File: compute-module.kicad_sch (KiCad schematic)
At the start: 16 parts, among them J7 DSI, SW1 SW_Push, SW2 SW_Push, U2 74154, U8 74LVC1G07SE-7

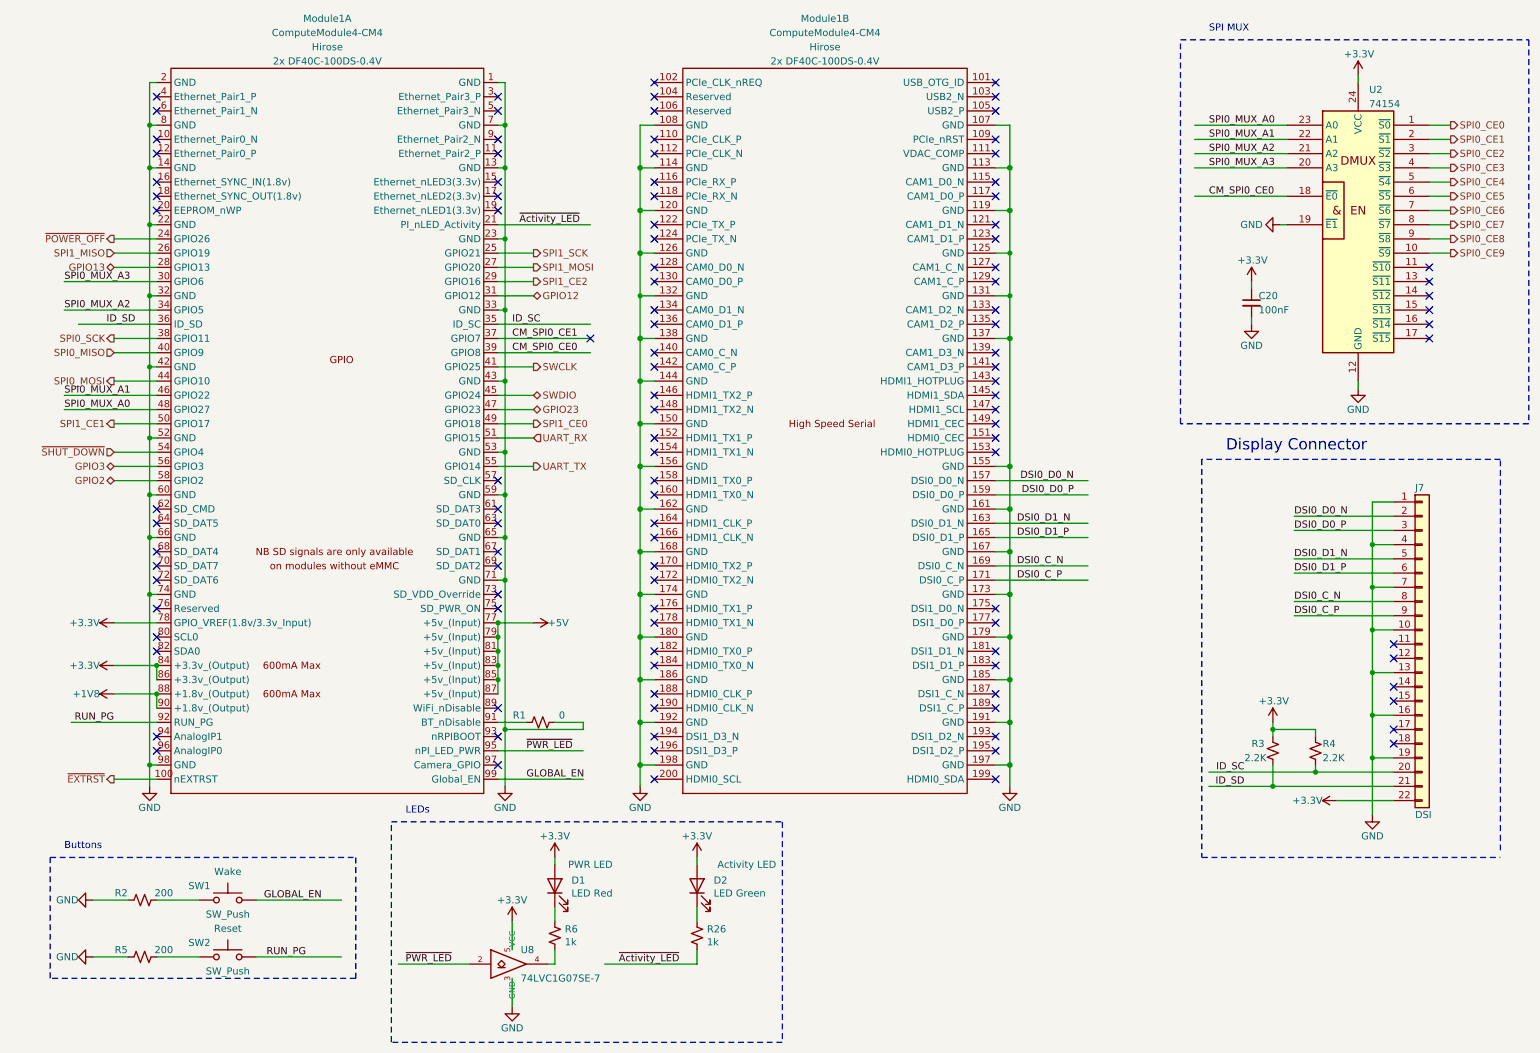
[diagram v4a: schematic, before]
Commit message: Assign some of the footprints and MPNs.
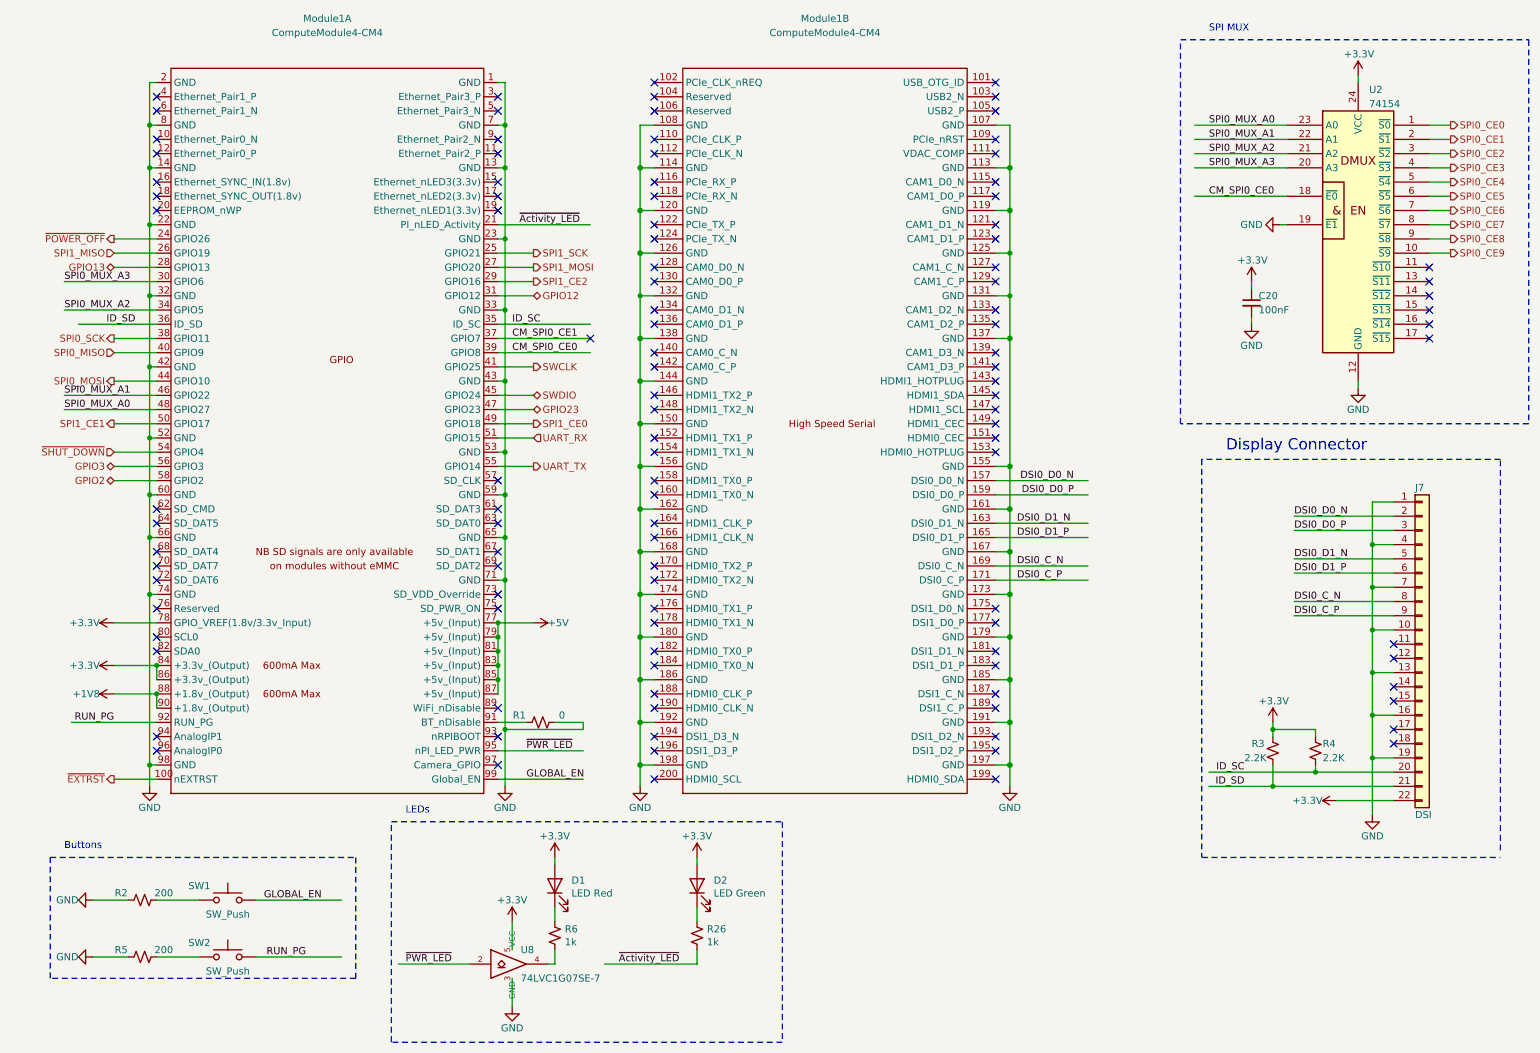
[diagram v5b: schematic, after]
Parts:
- C20: footprint (none) -> Capacitor_SMD:C_0402_1005Metric
- D1: Field4 Digikey -> (none); Field5 LTST-S270KRKT -> (none); Field6 SML-A12U8TT86Q -> (none); Field7 Rohm -> (none); Field8 650295101 -> (none); Function PWR LED -> (none); MPN (none) -> SML-A12U8TT86Q; Part Description Red 620nm LED Indication - Discrete 2.2V 2-SMD, No Lead -> (none)
- D2: Field4 Digikey -> (none); Field5 LTST-S270KGKT -> (none); Field6 SML-A12M8TT86N -> (none); Field7 Rohm -> (none); Field8 650263301 -> (none); Function Activity LED -> (none); MPN (none) -> SML-A12M8TT86N; Part Description Green 572nm LED Indication - Discrete 2.2V 2-SMD, No Lead -> (none)
- J7: Field4 Mouser -> (none); Field5 798-FH12-22S-0.5SH55 -> (none); Field6 FH12-22S-0.5SH55 -> (none); Field7 Hirose -> (none); MPN (none) -> FH12-22S-0.5SH55; Part Description 22 Position FFC, FPC Connector Contacts, Bottom 0.020" (0.5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 -> (none)
- Module1: Field4 Hirose -> (none); Field5 2x DF40C-100DS-0.4V -> (none)
- R1, R2, R5: footprint (none) -> Resistor_SMD:R_0402_1005Metric
- R26, R6: Field4 Farnell -> (none); Field5 9239235 -> (none); Field6 RK73H1ETTP1001F -> (none); Field7 KOA EUROPE GMBH -> (none); Field8 125049511 -> (none); MPN (none) -> RK73H1ETTP1001F; Part Description Resistor 1K M1005 1% 63mW -> (none)
- R3, R4: Field4 Farnell -> (none); Field5 9239278 -> (none); Field6 RK73G1ETQTP2201D -> (none); Field7 KOA EUROPE GMBH -> (none); Field8 120889581 -> (none); MPN (none) -> RK73G1ETQTP2201D; Part Description Resistor 2.2K M1005 1% 63mW -> (none)
- SW1: footprint (none) -> Button_Switch_SMD:SW_Push_1P1T_NO_6x6mm_H9.5mm; Function Wake -> (none); MPN (none) -> TS04-66-65-BK-100-SMT
- SW2: footprint (none) -> Button_Switch_SMD:SW_Push_1P1T_NO_6x6mm_H9.5mm; Function Reset -> (none); MPN (none) -> TS04-66-65-BK-100-SMT
- U8: Field4 Farnell -> (none); Field5 2425492 -> (none); Field6 74LVC1G07SE-7 -> (none); Field7 Diodes -> (none); MPN (none) -> 74LVC1G07SE-7; Part Description Buffer, Non-Inverting 1 Element 1 Bit per Element Open Drai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 -> (none)
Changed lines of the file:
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@@
       (effects (font (size 1.27 1.27)) hide)
     )
-    (property "Field4" "Mouser" (at 260.35 125.73 0)
-      (effects (font (size 1.27 1.27)) hide)
-    )
-    (property "Field5" "798-FH12-22S-0.5SH55" (at 260.35 125.73 0)
-      (effects (font (size 1.27 1.27)) hide)
-    )
-    (property "Field6" "FH12-22S-0.5SH55" (at 260.35 125.73 0)
-      (effects (font (size 1.27 1.27)) hide)
-    )
-    (property "Field7" "Hirose" (at 260.35 125.73 0)
-      (effects (font (size 1.27 1.27)) hide)
-    )
-    (property "Part Description" "22 Position FFC, FPC Connector Contacts, Bottom 0.020\" (0.50mm) Surface Mount, Right Angle" (at 260.35 125.73 0)
+    (property "MPN" "FH12-22S-0.5SH55" (at 260.35 125.73 0)
       (effects (font (size 1.27 1.27)) hide)
     )
@@
       (effects (font (size 1.27 1.27)) hide)
     )
-    (property "Field4" "Farnell" (at 241.3 144.78 0)
-      (effects (font (size 1.27 1.27)) hide)
-    )
-    (property "Field5" "9239278" (at 241.3 144.78 0)
-      (effects (font (size 1.27 1.27)) hide)
-    )
-    (property "Field7" "KOA EUROPE GMBH" (at 241.3 144.78 0)
-      (effects (font (size 1.27 1.27)) hide)
-    )
-    (property "Field6" "RK73G1ETQTP2201D         " (at 241.3 144.78 0)
-      (effects (font (size 1.27 1.27)) hide)
-    )
-    (property "Part Description" "Resistor 2.2K M1005 1% 63mW" (at 241.3 144.78 0)
-      (effects (font (size 1.27 1.27)) hide)
-    )
-    (property "Field8" "120889581" (at 241.3 144.78 0)
+    (property "MPN" "RK73G1ETQTP2201D         " (at 241.3 144.78 0)
       (effects (font (size 1.27 1.27)) hide)
     )
@@
       (effects (font (size 1.27 1.27)))
     )
-    (property "Footprint" "" (at 31.75 171.45 0)
+    (property "Footprint" "Resistor_SMD:R_0402_1005Metric" (at 31.75 171.45 0)
       (effects (font (size 1.27 1.27)) hide)
     )
@@
       (effects (font (size 1.27 1.27)) hide)
     )
-    (property "Field4" "Farnell" (at 130.81 177.8 0)
-      (effects (font (size 1.27 1.27)) hide)
-    )
-    (property "Field5" "9239235" (at 130.81 177.8 0)
-      (effects (font (size 1.27 1.27)) hide)
-    )
-    (property "Field7" "KOA EUROPE GMBH" (at 130.81 177.8 0)
-      (effects (font (size 1.27 1.27)) hide)
-    )
-    (property "Field6" "RK73H1ETTP1001F" (at 130.81 177.8 0)
-      (effects (font (size 1.27 1.27)) hide)
-    )
-    (property "Part Description" "Resistor 1K M1005 1% 63mW" (at 130.81 177.8 0)
-      (effects (font (size 1.27 1.27)) hide)
-    )
-    (property "Field8" "125049511" (at 130.81 177.8 0)
+    (property "MPN" "RK73H1ETTP1001F" (at 130.81 177.8 0)
       (effects (font (size 1.27 1.27)) hide)
     )
@@
       (effects (font (size 1.27 1.27)))
     )
-    (property "Footprint" "" (at 31.75 181.61 0)
+    (property "Footprint" "Resistor_SMD:R_0402_1005Metric" (at 31.75 181.61 0)
       (effects (font (size 1.27 1.27)) hide)
     )
@@
       (effects (font (size 1.27 1.27)) (justify left))
     )
-    (property "Footprint" "" (at 229.87 64.77 0)
+    (property "Footprint" "Capacitor_SMD:C_0402_1005Metric" (at 229.87 64.77 0)
       (effects (font (size 1.27 1.27)) hide)
     )
@@
       (effects (font (size 1.27 1.27)) hide)
     )
-    (property "Field4" "Digikey " (at 105.41 168.91 0)
-      (effects (font (size 1.27 1.27)) hide)
-    )
-    (property "Field5" "	LTST-S270KRKT" (at 105.41 168.91 0)
-      (effects (font (size 1.27 1.27)) hide)
-    )
-    (property "Field6" "SML-A12U8TT86Q" (at 105.41 168.91 0)
-      (effects (font (size 1.27 1.27)) hide)
-    )
-    (property "Field7" "Rohm" (at 105.41 168.91 0)
-      (effects (font (size 1.27 1.27)) hide)
-    )
-    (property "Field8" "650295101" (at 105.41 168.91 0)
-      (effects (font (size 1.27 1.27)) hide)
-    )
-    (property "Part Description" "	Red 620nm LED Indication - Discrete 2.2V 2-SMD, No Lead" (at 105.41 168.91 0)
-      (effects (font (size 1.27 1.27)) hide)
-    )
-    (property "Function" "PWR LED" (at 111.76 165.1 90)
-      (effects (font (size 1.27 1.27)))
+    (property "MPN" "SML-A12U8TT86Q" (at 105.41 168.91 0)
+      (effects (font (size 1.27 1.27)) hide)
     )
     (pin "1")
@@
       (effects (font (size 1.27 1.27)) hide)
     )
-    (property "Field4" "Farnell" (at 97.79 182.88 0)
-      (effects (font (size 1.27 1.27)) hide)
-    )
-    (property "Field5" "2425492" (at 97.79 182.88 0)
-      (effects (font (size 1.27 1.27)) hide)
-    )
-    (property "Field6" "74LVC1G07SE-7" (at 97.79 182.88 0)
-      (effects (font (size 1.27 1.27)) hide)
-    )
-    (property "Field7" "Diodes" (at 97.79 182.88 0)
-      (effects (font (size 1.27 1.27)) hide)
-    )
-    (property "Part Description" "Buffer, Non-Inverting 1 Element 1 Bit per Element Open Drain Output SOT-353" (at 97.79 182.88 0)
+    (property "MPN" "74LVC1G07SE-7" (at 97.79 182.88 0)
       (effects (font (size 1.27 1.27)) hide)
     )
@@
     (property "Datasheet" "" (at 156.21 113.03 0)
       (effects (font (size 1.27 1.27)) hide)
-    )
-    (property "Field4" "Hirose" (at 153.67 19.05 0)
-      (effects (font (size 1.27 1.27)))
-    )
-    (property "Field5" "2x DF40C-100DS-0.4V" (at 153.67 21.59 0)
-      (effects (font (size 1.27 1.27)))
     )
     (pin "1")
@@
       (effects (font (size 1.27 1.27)) hide)
     )
-    (property "Field4" "Hirose" (at 64.77 19.05 0)
-      (effects (font (size 1.27 1.27)))
-    )
-    (property "Field5" "2x DF40C-100DS-0.4V" (at 64.77 21.59 0)
-      (effects (font (size 1.27 1.27)))
-    )
     (pin "1")
     (pin "10")
@@
       (effects (font (size 1.27 1.27)))
     )
-    (property "Footprint" "" (at 46.99 176.53 0)
+    (property "Footprint" "Button_Switch_SMD:SW_Push_1P1T_NO_6x6mm_H9.5mm" (at 46.99 176.53 0)
       (effects (font (size 1.27 1.27)) hide)
     )
@@
       (effects (font (size 1.27 1.27)) hide)
     )
-    (property "Function" "Reset" (at 46.99 176.53 0)
-      (effects (font (size 1.27 1.27)))
+    (property "MPN" "TS04-66-65-BK-100-SMT" (at 46.99 181.61 0)
+      (effects (font (size 1.27 1.27)) hide)
     )
     (pin "1")
@@
       (effects (font (size 1.27 1.27)) hide)
     )
-    (property "Field4" "Digikey " (at 130.81 168.91 0)
-      (effects (font (size 1.27 1.27)) hide)
-    )
-    (property "Field5" "LTST-S270KGKT" (at 130.81 168.91 0)
-      (effects (font (size 1.27 1.27)) hide)
-    )
-    (property "Field6" "SML-A12M8TT86N" (at 130.81 168.91 0)
-      (effects (font (size 1.27 1.27)) hide)
-    )
-    (property "Field7" "Rohm" (at 130.81 168.91 0)
-      (effects (font (size 1.27 1.27)) hide)
-    )
-    (property "Field8" "650263301" (at 130.81 168.91 0)
-      (effects (font (size 1.27 1.27)) hide)
-    )
-    (property "Part Description" "	Green 572nm LED Indication - Discrete 2.2V 2-SMD, No Lead" (at 130.81 168.91 0)
-      (effects (font (size 1.27 1.27)) hide)
-    )
-    (property "Function" "Activity LED" (at 139.7 165.1 90)
-      (effects (font (size 1.27 1.27)))
+    (property "MPN" "SML-A12M8TT86N" (at 130.81 168.91 0)
+      (effects (font (size 1.27 1.27)) hide)
     )
     (pin "1")
@@
       (effects (font (size 1.27 1.27)))
     )
-    (property "Footprint" "" (at 46.99 166.37 0)
+    (property "Footprint" "Button_Switch_SMD:SW_Push_1P1T_NO_6x6mm_H9.5mm" (at 46.99 166.37 0)
       (effects (font (size 1.27 1.27)) hide)
     )
@@
       (effects (font (size 1.27 1.27)) hide)
     )
-    (property "Function" "Wake" (at 46.99 166.37 0)
-      (effects (font (size 1.27 1.27)))
+    (property "MPN" "TS04-66-65-BK-100-SMT" (at 46.99 171.45 0)
+      (effects (font (size 1.27 1.27)) hide)
     )
     (pin "1")
@@
       (effects (font (size 1.27 1.27)) hide)
     )
-    (property "Field4" "Farnell" (at 105.41 177.8 0)
-      (effects (font (size 1.27 1.27)) hide)
-    )
-    (property "Field5" "9239235" (at 105.41 177.8 0)
-      (effects (font (size 1.27 1.27)) hide)
-    )
-    (property "Field7" "KOA EUROPE GMBH" (at 105.41 177.8 0)
-      (effects (font (size 1.27 1.27)) hide)
-    )
-    (property "Field6" "RK73H1ETTP1001F" (at 105.41 177.8 0)
-      (effects (font (size 1.27 1.27)) hide)
-    )
-    (property "Part Description" "Resistor 1K M1005 1% 63mW" (at 105.41 177.8 0)
-      (effects (font (size 1.27 1.27)) hide)
-    )
-    (property "Field8" "125049511" (at 105.41 177.8 0)
+    (property "MPN" "RK73H1ETTP1001F" (at 105.41 177.8 0)
       (effects (font (size 1.27 1.27)) hide)
     )
@@
       (effects (font (size 1.27 1.27)) hide)
     )
-    (property "Field4" "Farnell" (at 233.68 144.78 0)
-      (effects (font (size 1.27 1.27)) hide)
-    )
-    (property "Field5" "9239278" (at 233.68 144.78 0)
-      (effects (font (size 1.27 1.27)) hide)
-    )
-    (property "Field7" "KOA EUROPE GMBH" (at 233.68 144.78 0)
-      (effects (font (size 1.27 1.27)) hide)
-    )
-    (property "Field6" "RK73G1ETQTP2201D         " (at 233.68 144.78 0)
-      (effects (font (size 1.27 1.27)) hide)
-    )
-    (property "Part Description" "Resistor 2.2K M1005 1% 63mW" (at 233.68 144.78 0)
-      (effects (font (size 1.27 1.27)) hide)
-    )
-    (property "Field8" "120889581" (at 233.68 144.78 0)
+    (property "MPN" "RK73G1ETQTP2201D         " (at 233.68 144.78 0)
       (effects (font (size 1.27 1.27)) hide)
     )
@@
       (effects (font (size 1.27 1.27)))
     )
-    (property "Footprint" "" (at 102.87 139.7 0)
-      (effects (font (size 1.27 1.27)) hide)
-    )
+    (property "Footprint" "Resistor_SMD:R_0402_1005Metric" (at 102.87 139.7 0)
+      (effects (font (size 1.27 1.27)) hide)
+    )

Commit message: Import the previous main board to match the overall shape, and re-annotate the schematic.
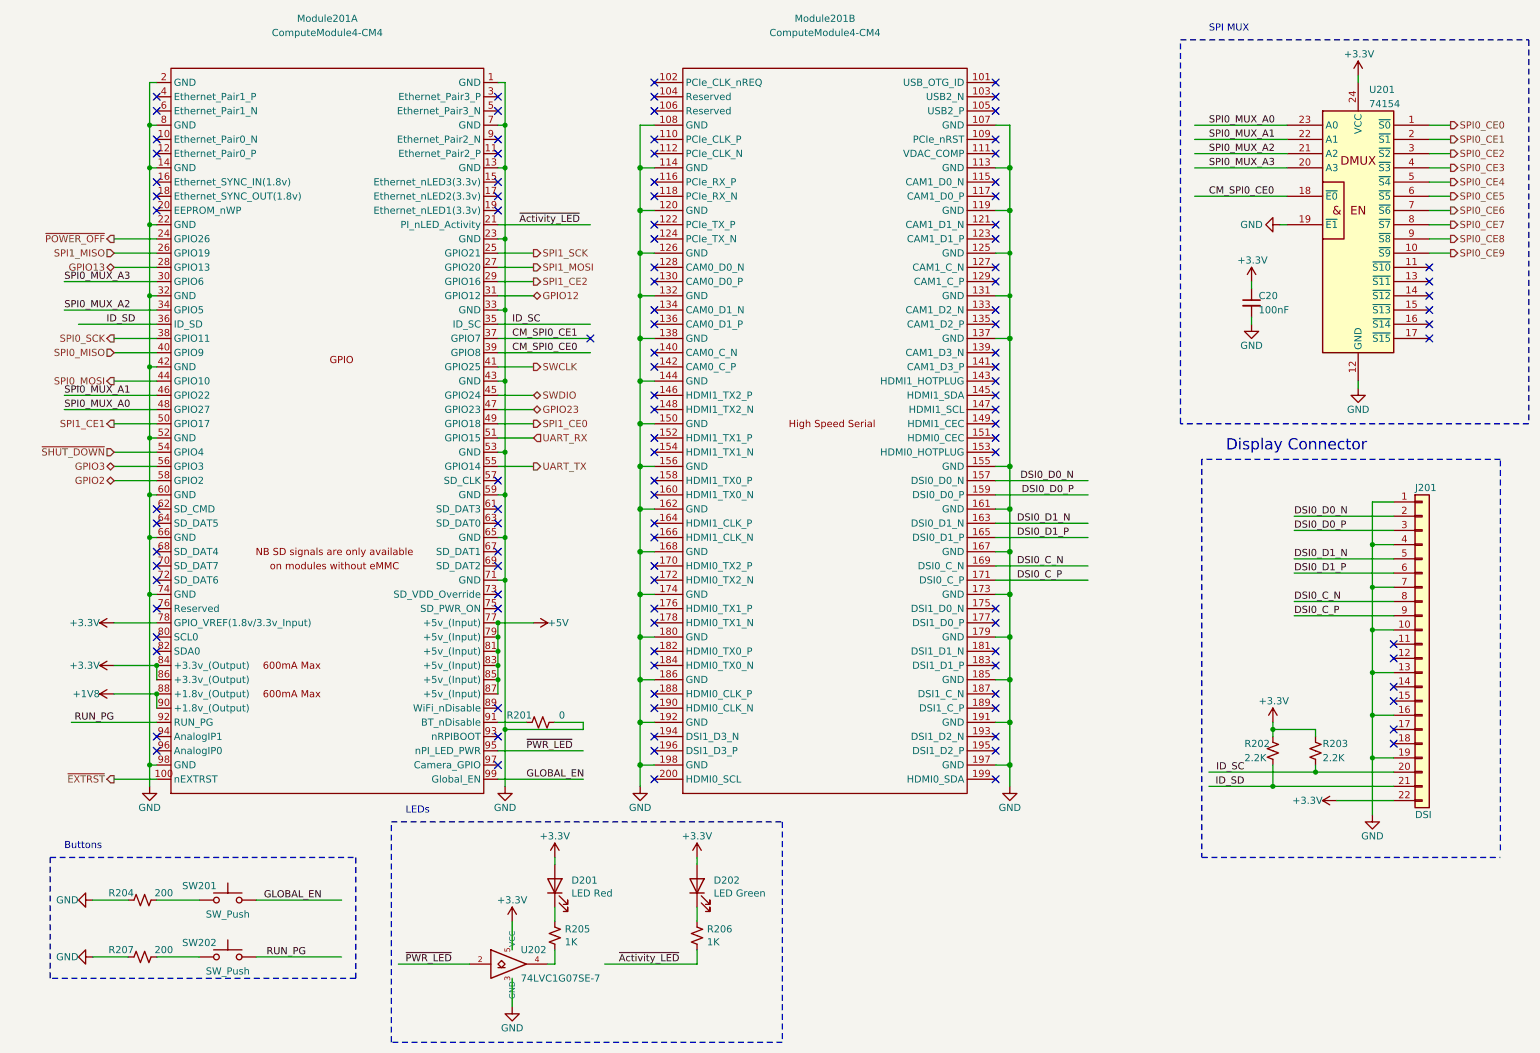
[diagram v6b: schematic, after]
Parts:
- C20: footprint Capacitor_SMD:C_0402_1005Metric -> Capacitor_SMD:C_0603_1608Metric; MPN (none) -> RM EMK105 B7104KV-F
- R201: renamed from R1; footprint Resistor_SMD:R_0402_1005Metric -> Resistor_SMD:R_0603_1608Metric; MPN (none) -> RMCF0603ZT0R00
- R202: renamed from R3; footprint Resistor_SMD:R_0402_1005Metric -> Resistor_SMD:R_0603_1608Metric; MPN RK73G1ETQTP2201D -> RC0603FR-132K2L
- R203: renamed from R4; footprint Resistor_SMD:R_0402_1005Metric -> Resistor_SMD:R_0603_1608Metric; MPN RK73G1ETQTP2201D -> RC0603FR-132K2L
- R204: renamed from R2; footprint Resistor_SMD:R_0402_1005Metric -> Resistor_SMD:R_0603_1608Metric; MPN (none) -> RC0603FR-13200RL
- R205: renamed from R6; value 1k -> 1K; footprint Resistor_SMD:R_0402_1005Metric -> Resistor_SMD:R_0603_1608Metric; MPN RK73H1ETTP1001F -> RC0603FR-101KL
- R206: renamed from R26; value 1k -> 1K; footprint Resistor_SMD:R_0402_1005Metric -> Resistor_SMD:R_0603_1608Metric; MPN RK73H1ETTP1001F -> RC0603FR-101KL
- R207: renamed from R5; footprint Resistor_SMD:R_0402_1005Metric -> Resistor_SMD:R_0603_1608Metric; MPN (none) -> RC0603FR-13200RL
- renumbered D1 to D201, D2 to D202, J7 to J201, Module1 to Module201, SW1 to SW201, SW2 to SW202, U2 to U201, U8 to U202
